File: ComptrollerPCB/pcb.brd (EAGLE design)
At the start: 160 x 100 mm, 35 parts, among them J1 FEMALE_HEADER_5X2, U1 ATMEGA32U4, X1 16MHz

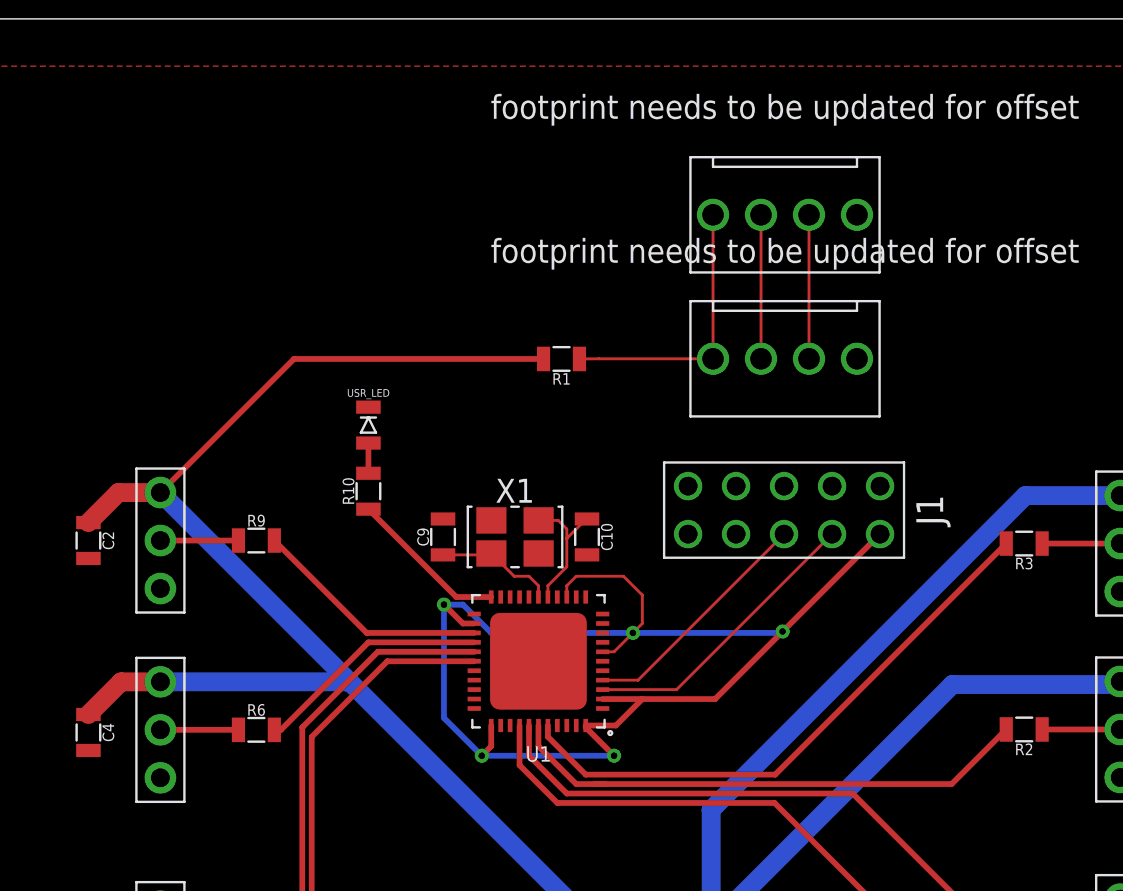
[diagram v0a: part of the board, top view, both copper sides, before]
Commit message: analog additions to read temperatures
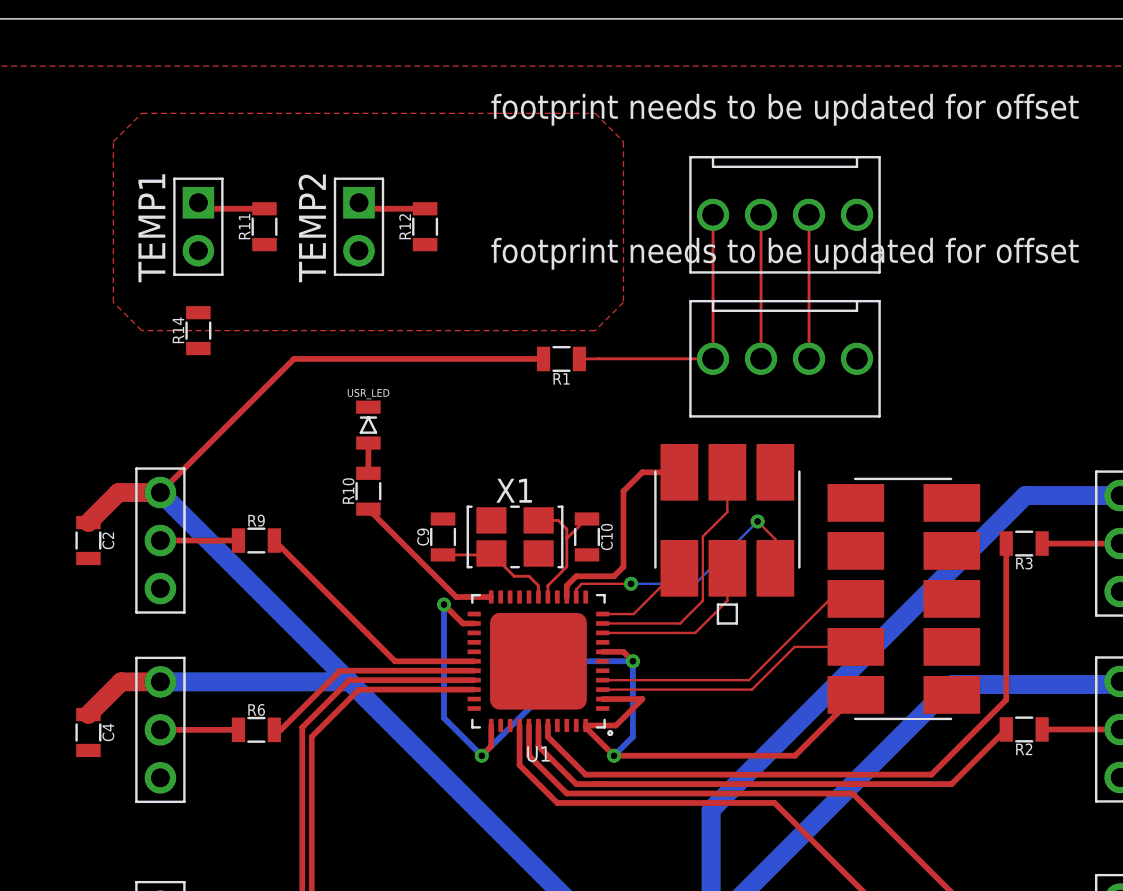
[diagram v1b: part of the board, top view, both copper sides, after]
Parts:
- added J2: ISP_CONN_6PIN, connectors:3X2_HEADER_SMT
- added R11, R12, R14: (no value), passive:0805
- added TEMP1, TEMP2: FEMALE_HEADER_2X1, connectors:2X1_HEADER
- J1: value FEMALE_HEADER_5X2 -> FEMALE_HEADER_5X2SMT; device connectors:5X2_HEADER -> connectors:5X2_HEADER_SMT
- moved J1 7.86 mm to (86.3, 69.3), turned to 90 degrees
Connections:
- new net AGND: R14.2, TEMP1.3, TEMP2.3
- new net MISO: J2.1, U1.11
- new net MOSI: J2.4, U1.10
- new net N$11: U1.26
- new net N$12: U1.27
- new net SCK: J2.3, U1.9
- new net TEMP1: R11.2, TEMP1.1
- new net TEMP2: R12.2, TEMP2.1
- net GND: now also J2.6, R14.1
- net LED_5: now also U1.31; no longer U1.28
- net LED_6: now also U1.30; no longer U1.27
- net LED_7: now also U1.29; no longer U1.26
- net LED_8: now also U1.28; no longer U1.25
- net USB_5V: now also J2.2, R11.1, R12.1
- net _RESET: now also J2.5
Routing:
- net _RESET: track 0.00 -> 14.4 mm, vias 0 -> 2
- net MOSI: track 0.00 -> 13.1 mm
- net SCK: track 0.00 -> 9.02 mm
- net USB_5V: track 71.8 -> 63.4 mm, vias 5 -> 4
- net MISO: track 0.00 -> 5.06 mm
- net LED_1: track 30.8 -> 35.6 mm
- net TEMP2: track 0.00 -> 3.63 mm
- net TEMP1: track 0.00 -> 3.52 mm
- net USB_D+: track 12.8 -> 15.2 mm
- net USB_D-: track 15.5 -> 14.3 mm
- net LED_5: track 33.3 -> 32.7 mm
- net LED_7: track 12.5 -> 11.9 mm
- net LED_8: track 12.6 -> 13.2 mm
- net LED_6: track 23.4 -> 22.8 mm
- added copper zone on layer 1, net AGND
